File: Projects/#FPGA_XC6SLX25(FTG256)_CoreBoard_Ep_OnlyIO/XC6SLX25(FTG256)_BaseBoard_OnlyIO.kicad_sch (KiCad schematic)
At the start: 3 parts, among them J1 2309411-1, J2 Conn_01x30, J3 Conn_01x30

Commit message: update FPGA_XC6SLX25_BaseBoard_OnlyIO
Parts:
- added J4, J5: Conn_01x30, Connector_PinSocket_2.54mm:PinSocket_1x30_P2.54mm_Vertical, symbol Connector_Generic:Conn_01x30
- J2, J3: footprint (none) -> Connector_PinSocket_2.54mm:PinSocket_1x30_P2.54mm_Vertical
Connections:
- net Bank0_L1-: now also J4.25 (Pin_25)
- net Bank0_L2+: now also J4.21 (Pin_21)
- net Bank0_L2-: now also J4.22 (Pin_22)
- net Bank0_L3+: now also J4.24 (Pin_24)
- net Bank0_L3-: now also J4.23 (Pin_23)
- net Bank0_L33+: now also J4.16 (Pin_16)
- net Bank0_L33-: now also J4.15 (Pin_15)
- net Bank0_L34+: now also J4.14 (Pin_14)
- net Bank0_L34-: now also J4.13 (Pin_13)
- net Bank0_L35+: now also J4.11 (Pin_11)
- net Bank0_L35-: now also J4.12 (Pin_12)
- net Bank0_L36+: now also J5.11 (Pin_11)
- net Bank0_L36-: now also J5.10 (Pin_10)
- net Bank0_L37+: now also J5.4 (Pin_4)
- net Bank0_L37-: now also J5.5 (Pin_5)
- net Bank0_L38+: now also J5.8 (Pin_8)
- net Bank0_L38-: now also J5.9 (Pin_9)
- net Bank0_L39+: now also J4.10 (Pin_10)
- net Bank0_L39-: now also J4.9 (Pin_9)
- net Bank0_L4+: now also J4.20 (Pin_20)
- net Bank0_L4-: now also J4.19 (Pin_19)
- net Bank0_L40+: now also J5.7 (Pin_7)
- net Bank0_L40-: now also J5.6 (Pin_6)
- net Bank0_L5+: now also J5.13 (Pin_13)
- net Bank0_L5-: now also J5.12 (Pin_12)
- net Bank0_L6+: now also J4.17 (Pin_17)
- net Bank0_L6-: now also J4.18 (Pin_18)
- net Bank0_L62+: now also J4.7 (Pin_7)
- net Bank0_L62-: now also J4.8 (Pin_8)
- net Bank0_L63+: now also J3.29 (Pin_29)
- net Bank0_L63-: now also J3.28 (Pin_28)
- net Bank0_L64+: now also J5.3 (Pin_3)
- net Bank0_L64-: now also J5.2 (Pin_2)
- net Bank0_L65+: now also J4.5 (Pin_5)
- net Bank0_L65-: now also J4.6 (Pin_6)
- net Bank0_L66+: now also J5.1 (Pin_1)
- net Bank0_L66-: now also J3.30 (Pin_30)
- net Bank0_L7+: now also J5.15 (Pin_15)
- net Bank0_L7-: now also J5.14 (Pin_14)
- net Bank1_L29+: now also J4.4 (Pin_4)
- net Bank1_L29-: now also J4.3 (Pin_3)
- net Bank1_L30+: now also J3.24 (Pin_24)
- net Bank1_L30-: now also J3.25 (Pin_25)
- net Bank1_L32+: now also J3.23 (Pin_23)
- net Bank1_L32-: now also J3.22 (Pin_22)
- net Bank1_L33+: now also J4.2 (Pin_2)
- net Bank1_L33-: now also J4.1 (Pin_1)
- net Bank1_L38+: now also J3.26 (Pin_26)
- net Bank1_L38-: now also J3.27 (Pin_27)
- net Bank1_L39+: now also J3.19 (Pin_19)
- net Bank1_L39-: now also J3.18 (Pin_18)
- net Bank1_L40+: now also J3.21 (Pin_21)
- net Bank1_L40-: now also J3.20 (Pin_20)
- net Bank1_L41+: now also J3.15 (Pin_15)
- net Bank1_L41-: now also J3.14 (Pin_14)
- net Bank1_L42+: now also J3.16 (Pin_16)
- net Bank1_L42-: now also J3.17 (Pin_17)
- net Bank1_L53+: now also J3.13 (Pin_13)
- net Bank1_L53-: now also J3.12 (Pin_12)
- net Bank1_L74+: now also J3.11 (Pin_11)
- net Bank1_L74-: now also J3.10 (Pin_10)
- net Bank2_L13-: now also J3.5 (Pin_5)
- net Bank2_L14+: now also J4.28 (Pin_28)
- net Bank2_L14-: now also J4.29 (Pin_29)
- net Bank2_L16+: now also J5.22 (Pin_22)
- net Bank2_L16-: now also J5.23 (Pin_23)
- net Bank2_L23+: now also J4.30 (Pin_30)
- net Bank2_L23-: now also J5.19 (Pin_19)
- net Bank2_L29+: now also J4.26 (Pin_26)
- net Bank2_L29-: now also J4.27 (Pin_27)
- net Bank2_L30+: now also J5.21 (Pin_21)
- net Bank2_L30-: now also J5.20 (Pin_20)
- net Bank2_L31+: now also J5.24 (Pin_24)
- net Bank2_L31-: now also J5.25 (Pin_25)
- net Bank2_L32+: now also J3.3 (Pin_3)
- net Bank2_L47+: now also J3.6 (Pin_6)
- net Bank2_L47-: now also J3.2 (Pin_2)
- net Bank2_L48+: now also J3.4 (Pin_4)
- net Bank2_L48-: now also J5.30 (Pin_30)
- net Bank2_L49+: now also J5.29 (Pin_29)
- net Bank2_L49-: now also J5.28 (Pin_28)
- net Bank2_L62+: now also J5.26 (Pin_26)
- net Bank2_L62-: now also J5.27 (Pin_27)
- net Bank2_L63+: now also J3.9 (Pin_9)
- net Bank2_L63-: now also J3.1 (Pin_1)
- net Bank2_L64+: now also J3.8 (Pin_8)
- net Bank2_L64-: now also J3.7 (Pin_7)

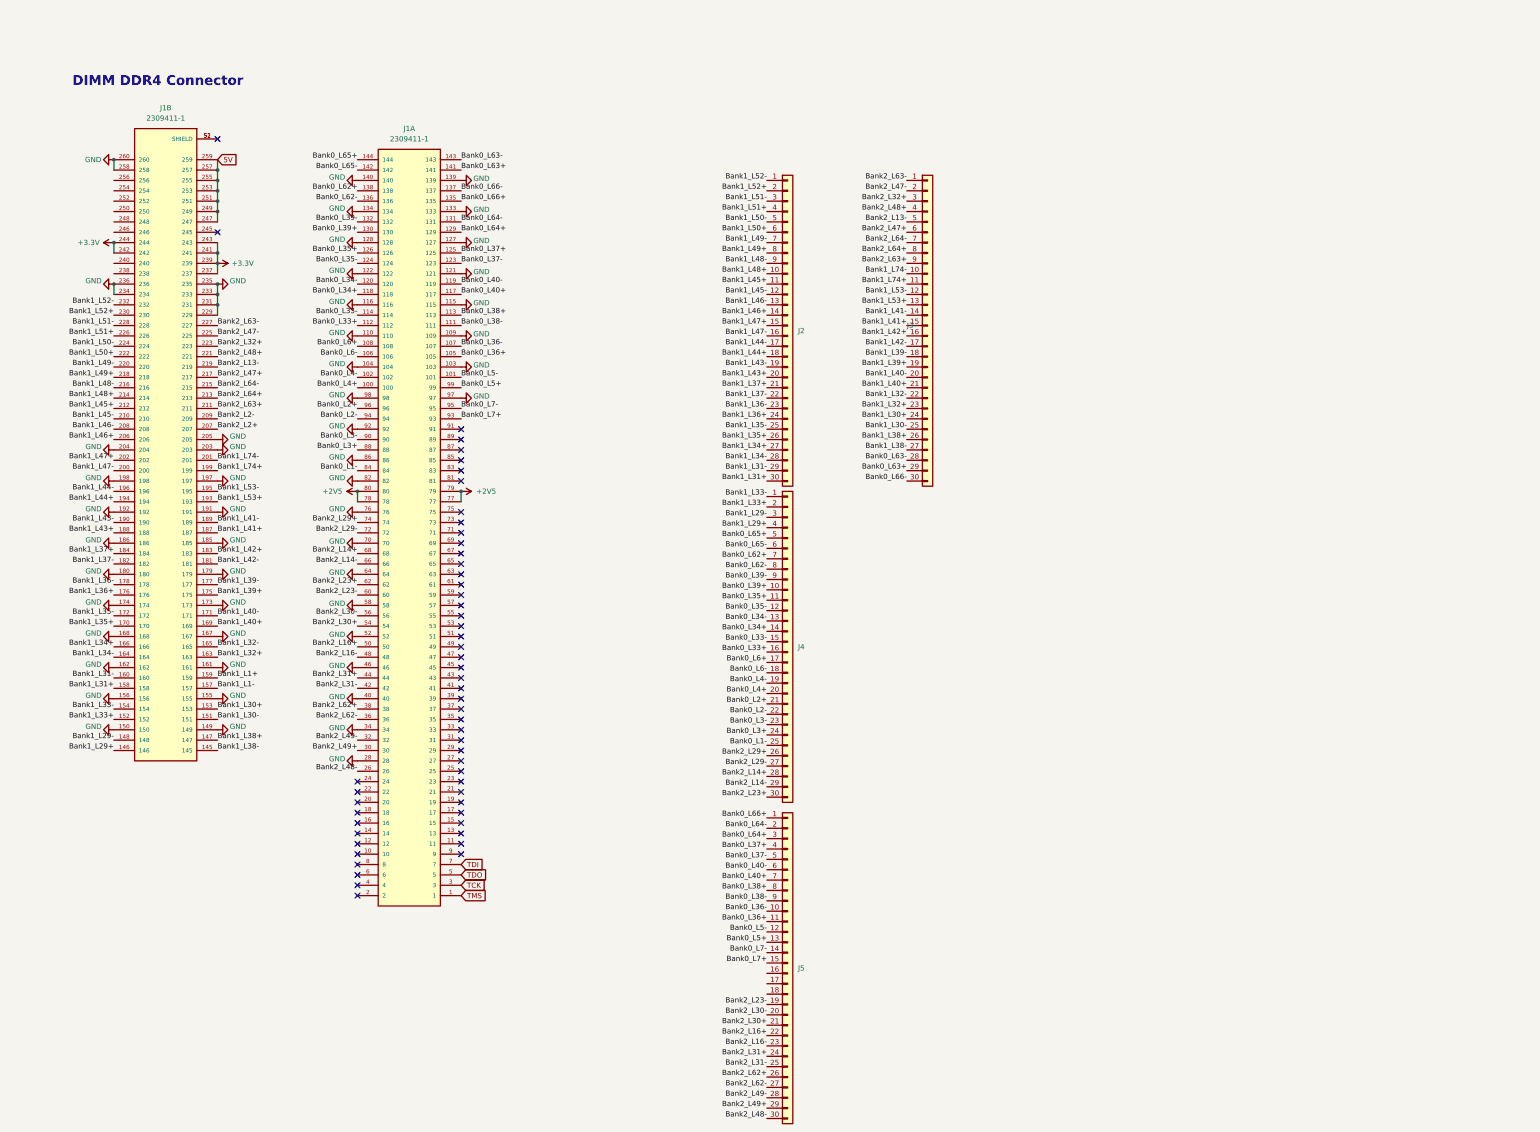
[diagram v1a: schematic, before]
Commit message: finish XC6SLX25(FTG256)_BaseBoard_OnlyIO (sample)
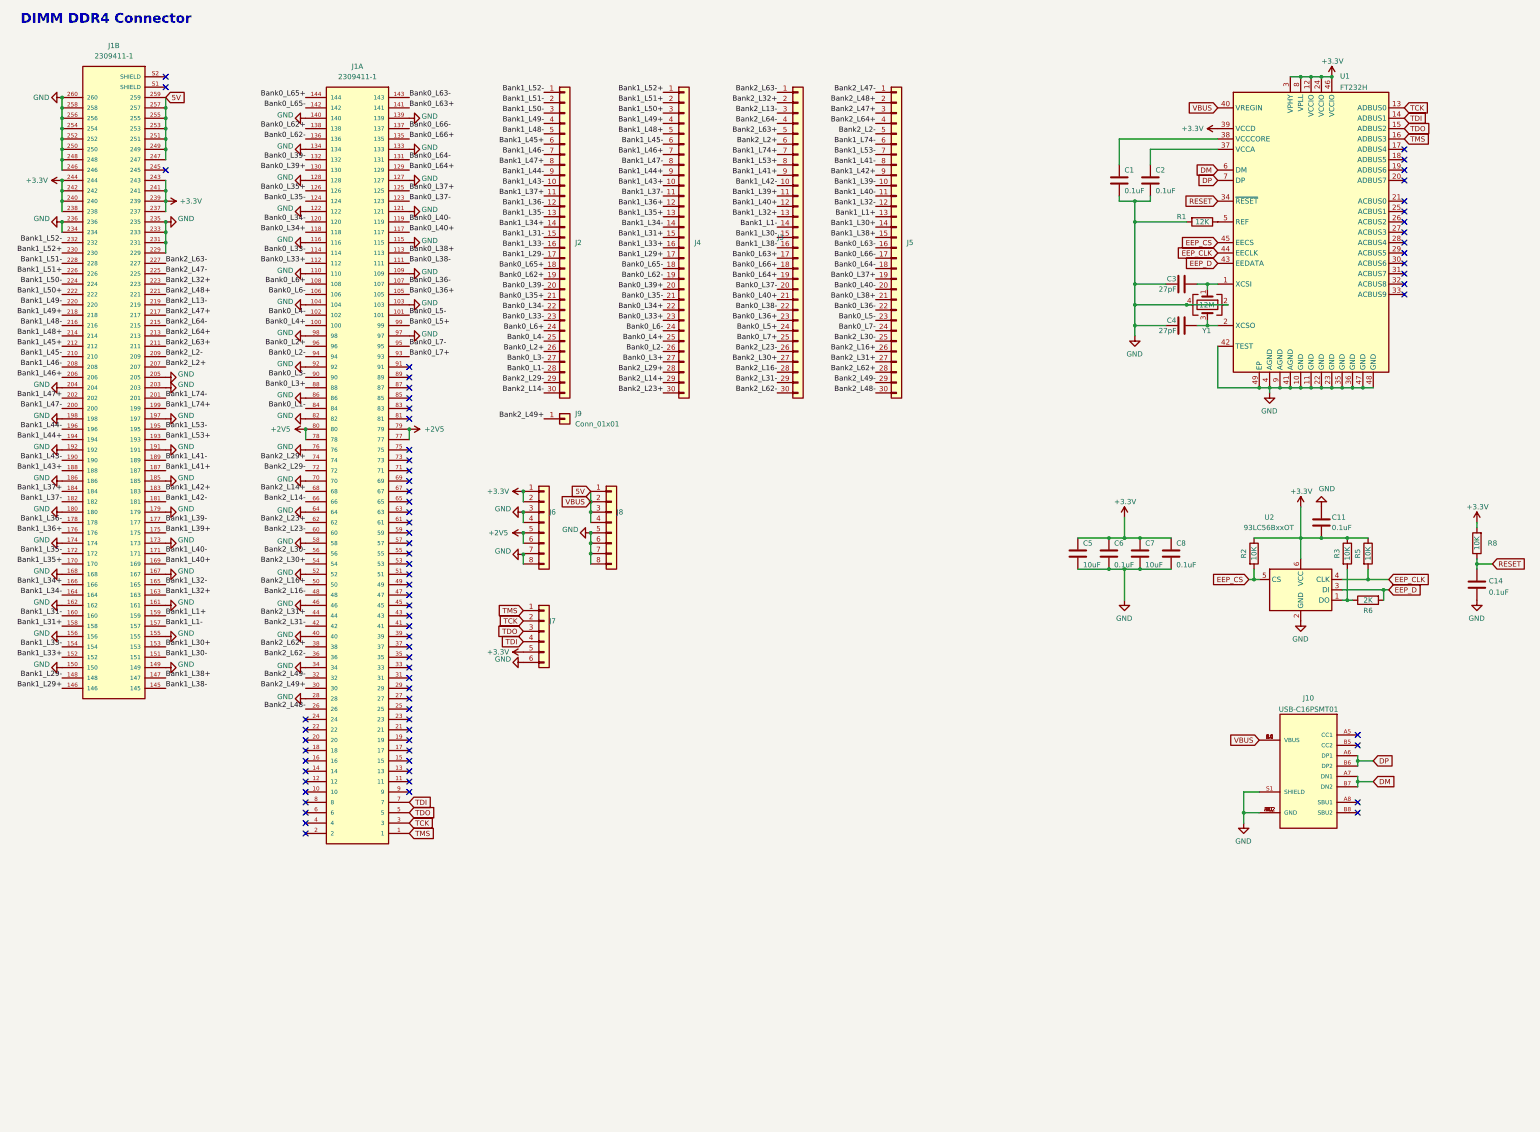
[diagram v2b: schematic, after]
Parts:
- added C1, C11, C14, C2, C6, C8: 0.1uF, Capacitor_SMD:C_0402_1005Metric, symbol Device:C
- added C3, C4: 27pF, Capacitor_SMD:C_0402_1005Metric, symbol Device:C
- added C5, C7: 10uF, Capacitor_SMD:C_0402_1005Metric, symbol Device:C
- added J10: USB-C16PSMT01, Connector_USB:USB_C_Receptacle_XKB_U262-16XN-4BVC11, symbol USB-C16PSMT01:CQ-USB-C16PSMT01
- added J6, J8: Conn_01x08, Connector_PinHeader_2.54mm:PinHeader_1x08_P2.54mm_Vertical, symbol Connector_Generic:Conn_01x08
- added J7: Conn_01x06, Connector_PinHeader_2.54mm:PinHeader_1x06_P2.54mm_Vertical, symbol Connector_Generic:Conn_01x06
- added J9: Conn_01x01, Connector_PinHeader_2.54mm:PinHeader_1x01_P2.54mm_Vertical, symbol Connector_Generic:Conn_01x01
- added R1: 12K, Resistor_SMD:R_0402_1005Metric, symbol Device:R
- added R2, R3, R5, R8: 10K, Resistor_SMD:R_0402_1005Metric, symbol Device:R
- added R6: 2K, Resistor_SMD:R_0402_1005Metric, symbol Device:R
- added U1: FT232H, Package_DFN_QFN:QFN-48-1EP_8x8mm_P0.5mm_EP6.2x6.2mm, symbol Interface_USB:FT232H
- added U2: 93LC56BxxOT, Package_TO_SOT_SMD:SOT-23-6, symbol Memory_EEPROM:93LCxxBxxOT
- added Y1: 12M, Crystal:Crystal_SMD_2016-4Pin_2.0x1.6mm, symbol Device:Crystal_GND24
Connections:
- net +2V5: now also J6.5 (Pin_5), J6.6 (Pin_6)
- net +3V3: now also J1.238, J1.240, C11.1, C5.1, C6.1, C7.1, C8.1, J6.1 (Pin_1), J6.2 (Pin_2), J7.5 (Pin_5), R2.1, R3.1, R5.1, R8.2, U1.12 (VCCIO), U1.24 (VCCIO), U1.3 (VPHY), U1.39 (VCCD), U1.46 (VCCIO), U1.8 (VPLL), U2.6 (VCC)
- net 5V: now also J10.A4 (VBUS), J10.A9 (VBUS), J10.B4 (VBUS), J10.B9 (VBUS), J8.1 (Pin_1), J8.2 (Pin_2), J8.3 (Pin_3), J8.4 (Pin_4), U1.40 (VREGIN)
- net Bank0_L1-: now also J2.28 (Pin_28); no longer J4.25 (Pin_25)
- net Bank0_L2+: now also J2.26 (Pin_26); no longer J4.21 (Pin_21)
- net Bank0_L2-: now also J4.26 (Pin_26); no longer J4.22 (Pin_22)
- net Bank0_L3+: now also J4.27 (Pin_27); no longer J4.24 (Pin_24)
- net Bank0_L3-: now also J2.27 (Pin_27); no longer J4.23 (Pin_23)
- net Bank0_L33+: now also J4.23 (Pin_23); no longer J4.16 (Pin_16)
- net Bank0_L33-: now also J2.23 (Pin_23); no longer J4.15 (Pin_15)
- net Bank0_L34+: now also J4.22 (Pin_22); no longer J4.14 (Pin_14)
- net Bank0_L34-: now also J2.22 (Pin_22); no longer J4.13 (Pin_13)
- net Bank0_L35+: now also J2.21 (Pin_21); no longer J4.11 (Pin_11)
- net Bank0_L35-: now also J4.21 (Pin_21); no longer J4.12 (Pin_12)
- net Bank0_L36+: now also J3.23 (Pin_23); no longer J5.11 (Pin_11)
- net Bank0_L36-: now also J5.22 (Pin_22); no longer J5.10 (Pin_10)
- net Bank0_L37+: now also J5.19 (Pin_19); no longer J5.4 (Pin_4)
- net Bank0_L37-: now also J3.20 (Pin_20); no longer J5.5 (Pin_5)
- net Bank0_L38+: now also J5.21 (Pin_21); no longer J5.8 (Pin_8)
- net Bank0_L38-: now also J3.22 (Pin_22); no longer J5.9 (Pin_9)
- net Bank0_L39+: now also J4.20 (Pin_20); no longer J4.10 (Pin_10)
- net Bank0_L39-: now also J2.20 (Pin_20); no longer J4.9 (Pin_9)
- net Bank0_L4+: now also J4.25 (Pin_25); no longer J4.20 (Pin_20)
- net Bank0_L4-: now also J2.25 (Pin_25); no longer J4.19 (Pin_19)
- net Bank0_L40+: now also J3.21 (Pin_21); no longer J5.7 (Pin_7)
- net Bank0_L40-: now also J5.20 (Pin_20); no longer J5.6 (Pin_6)
- net Bank0_L5+: now also J3.24 (Pin_24); no longer J5.13 (Pin_13)
- net Bank0_L5-: now also J5.23 (Pin_23); no longer J5.12 (Pin_12)
- net Bank0_L6+: now also J2.24 (Pin_24); no longer J4.17 (Pin_17)
- net Bank0_L6-: now also J4.24 (Pin_24); no longer J4.18 (Pin_18)
- net Bank0_L62+: now also J2.19 (Pin_19); no longer J4.7 (Pin_7)
- net Bank0_L62-: now also J4.19 (Pin_19); no longer J4.8 (Pin_8)
- net Bank0_L63+: now also J3.17 (Pin_17); no longer J3.29 (Pin_29)
- net Bank0_L63-: now also J5.16 (Pin_16); no longer J3.28 (Pin_28)
- net Bank0_L64+: now also J3.19 (Pin_19); no longer J5.3 (Pin_3)
- net Bank0_L64-: now also J5.18 (Pin_18); no longer J5.2 (Pin_2)
- net Bank0_L65+: now also J2.18 (Pin_18); no longer J4.5 (Pin_5)
- net Bank0_L65-: now also J4.18 (Pin_18); no longer J4.6 (Pin_6)
- net Bank0_L66+: now also J3.18 (Pin_18); no longer J5.1 (Pin_1)
- net Bank0_L66-: now also J5.17 (Pin_17); no longer J3.30 (Pin_30)
- net Bank0_L7+: now also J3.25 (Pin_25); no longer J5.15 (Pin_15)
- net Bank0_L7-: now also J5.24 (Pin_24); no longer J5.14 (Pin_14)
- net Bank1_L1+: now also J5.13 (Pin_13)
- net Bank1_L1-: now also J3.14 (Pin_14)
- net Bank1_L29+: now also J4.17 (Pin_17); no longer J4.4 (Pin_4)
- net Bank1_L29-: now also J2.17 (Pin_17); no longer J4.3 (Pin_3)
- net Bank1_L30+: now also J5.14 (Pin_14); no longer J3.24 (Pin_24)
- net Bank1_L30-: now also J3.15 (Pin_15); no longer J3.25 (Pin_25)
- net Bank1_L31+: now also J4.15 (Pin_15); no longer J2.30 (Pin_30)
- net Bank1_L31-: now also J2.15 (Pin_15); no longer J2.29 (Pin_29)
- net Bank1_L32+: now also J3.13 (Pin_13); no longer J3.23 (Pin_23)
- net Bank1_L32-: now also J5.12 (Pin_12); no longer J3.22 (Pin_22)
- net Bank1_L33+: now also J4.16 (Pin_16); no longer J4.2 (Pin_2)
- net Bank1_L33-: now also J2.16 (Pin_16); no longer J4.1 (Pin_1)
- net Bank1_L34+: now also J2.14 (Pin_14); no longer J2.27 (Pin_27)
- net Bank1_L34-: now also J4.14 (Pin_14); no longer J2.28 (Pin_28)
- net Bank1_L35+: now also J4.13 (Pin_13); no longer J2.26 (Pin_26)
- net Bank1_L35-: now also J2.13 (Pin_13); no longer J2.25 (Pin_25)
- net Bank1_L36+: now also J4.12 (Pin_12); no longer J2.24 (Pin_24)
- net Bank1_L36-: now also J2.12 (Pin_12); no longer J2.23 (Pin_23)
- net Bank1_L37+: now also J2.11 (Pin_11); no longer J2.21 (Pin_21)
- net Bank1_L37-: now also J4.11 (Pin_11); no longer J2.22 (Pin_22)
- net Bank1_L38+: now also J5.15 (Pin_15); no longer J3.26 (Pin_26)
- net Bank1_L38-: now also J3.16 (Pin_16); no longer J3.27 (Pin_27)
- net Bank1_L39+: now also J3.11 (Pin_11); no longer J3.19 (Pin_19)
- net Bank1_L39-: now also J5.10 (Pin_10); no longer J3.18 (Pin_18)
- net Bank1_L40+: now also J3.12 (Pin_12); no longer J3.21 (Pin_21)
- net Bank1_L40-: now also J5.11 (Pin_11); no longer J3.20 (Pin_20)
- net Bank1_L41+: now also J3.9 (Pin_9); no longer J3.15 (Pin_15)
- net Bank1_L41-: now also J5.8 (Pin_8); no longer J3.14 (Pin_14)
- net Bank1_L42+: now also J5.9 (Pin_9); no longer J3.16 (Pin_16)
- net Bank1_L42-: now also J3.10 (Pin_10); no longer J3.17 (Pin_17)
- net Bank1_L43+: now also J4.10 (Pin_10); no longer J2.20 (Pin_20)
- net Bank1_L43-: now also J2.10 (Pin_10); no longer J2.19 (Pin_19)
- net Bank1_L44+: now also J4.9 (Pin_9); no longer J2.18 (Pin_18)
- net Bank1_L44-: now also J2.9 (Pin_9); no longer J2.17 (Pin_17)
- net Bank1_L45+: now also J2.6 (Pin_6); no longer J2.11 (Pin_11)
- net Bank1_L45-: now also J4.6 (Pin_6); no longer J2.12 (Pin_12)
- net Bank1_L46+: now also J4.7 (Pin_7); no longer J2.14 (Pin_14)
- net Bank1_L46-: now also J2.7 (Pin_7); no longer J2.13 (Pin_13)
- net Bank1_L47+: now also J2.8 (Pin_8); no longer J2.15 (Pin_15)
- net Bank1_L47-: now also J4.8 (Pin_8); no longer J2.16 (Pin_16)
- net Bank1_L48+: now also J4.5 (Pin_5); no longer J2.10 (Pin_10)
- net Bank1_L48-: now also J2.5 (Pin_5); no longer J2.9 (Pin_9)
- net Bank1_L49+: now also J4.4 (Pin_4); no longer J2.8 (Pin_8)
- net Bank1_L49-: now also J2.4 (Pin_4); no longer J2.7 (Pin_7)
- net Bank1_L50+: now also J4.3 (Pin_3); no longer J2.6 (Pin_6)
- net Bank1_L50-: now also J2.3 (Pin_3); no longer J2.5 (Pin_5)
- net Bank1_L51+: now also J4.2 (Pin_2); no longer J2.4 (Pin_4)
- net Bank1_L51-: now also J2.2 (Pin_2); no longer J2.3 (Pin_3)
- net Bank1_L52+: now also J4.1 (Pin_1); no longer J2.2 (Pin_2)
- net Bank1_L53+: now also J3.8 (Pin_8); no longer J3.13 (Pin_13)
- net Bank1_L53-: now also J5.7 (Pin_7); no longer J3.12 (Pin_12)
- net Bank1_L74+: now also J3.7 (Pin_7); no longer J3.11 (Pin_11)
- net Bank1_L74-: now also J5.6 (Pin_6); no longer J3.10 (Pin_10)
- net Bank2_L13-: now also J3.3 (Pin_3); no longer J3.5 (Pin_5)
- net Bank2_L14+: now also J4.29 (Pin_29); no longer J4.28 (Pin_28)
- net Bank2_L14-: now also J2.30 (Pin_30); no longer J4.29 (Pin_29)
- net Bank2_L16+: now also J5.26 (Pin_26); no longer J5.22 (Pin_22)
- net Bank2_L16-: now also J3.28 (Pin_28); no longer J5.23 (Pin_23)
- net Bank2_L2+: now also J3.6 (Pin_6)
- net Bank2_L2-: now also J5.5 (Pin_5)
- net Bank2_L23-: now also J3.26 (Pin_26); no longer J5.19 (Pin_19)
- net Bank2_L29+: now also J4.28 (Pin_28); no longer J4.26 (Pin_26)
- net Bank2_L29-: now also J2.29 (Pin_29); no longer J4.27 (Pin_27)
- net Bank2_L30+: now also J3.27 (Pin_27); no longer J5.21 (Pin_21)
- net Bank2_L30-: now also J5.25 (Pin_25); no longer J5.20 (Pin_20)
- net Bank2_L31+: now also J5.27 (Pin_27); no longer J5.24 (Pin_24)
- net Bank2_L31-: now also J3.29 (Pin_29); no longer J5.25 (Pin_25)
- net Bank2_L32+: now also J3.2 (Pin_2); no longer J3.3 (Pin_3)
- net Bank2_L47+: now also J5.3 (Pin_3); no longer J3.6 (Pin_6)
- net Bank2_L47-: now also J5.1 (Pin_1); no longer J3.2 (Pin_2)
- net Bank2_L48+: now also J5.2 (Pin_2); no longer J3.4 (Pin_4)
- net Bank2_L49+: now also J9.1 (Pin_1); no longer J5.29 (Pin_29)
- net Bank2_L49-: now also J5.29 (Pin_29); no longer J5.28 (Pin_28)
- net Bank2_L62+: now also J5.28 (Pin_28); no longer J5.26 (Pin_26)
- net Bank2_L62-: now also J3.30 (Pin_30); no longer J5.27 (Pin_27)
- net Bank2_L63+: now also J3.5 (Pin_5); no longer J3.9 (Pin_9)
- net Bank2_L64+: now also J5.4 (Pin_4); no longer J3.8 (Pin_8)
- net Bank2_L64-: now also J3.4 (Pin_4); no longer J3.7 (Pin_7)
- net GND: now also J1.246, J1.248, J1.250, J1.252, J1.254, J1.256, C1.2, C11.2, C14.2, C2.2, C3.1, C4.1, C5.2, C6.2, C7.2, C8.2, J10.A1 (GND), J10.A12 (GND), J10.B1 (GND), J10.B12 (GND), J10.S1 (SHIELD), J6.3 (Pin_3), J6.4 (Pin_4), J6.7 (Pin_7), J6.8 (Pin_8), J7.6 (Pin_6), J8.5 (Pin_5), J8.6 (Pin_6), J8.7 (Pin_7), J8.8 (Pin_8), R1.2, U1.10 (GND), U1.11 (GND), U1.22 (GND), U1.23 (GND), U1.35 (GND), U1.36 (GND), U1.4 (AGND), U1.41 (AGND), U1.42 (TEST), U1.47 (GND), U1.48 (GND), U1.49 (EP), U1.9 (AGND), U2.2 (GND), Y1.2, Y1.4
- net TCK: now also J7.2 (Pin_2), U1.13 (ADBUS0)
- net TDI: now also J7.4 (Pin_4), U1.14 (ADBUS1)
- net TDO: now also J7.3 (Pin_3), U1.15 (ADBUS2)
- net TMS: now also J7.1 (Pin_1), U1.16 (ADBUS3)
- net at J1.S1 (SHIELD): no longer J1.S2 (SHIELD)
- new net: C1.1, U1.38 (VCCCORE)
- new net: C3.2, U1.1 (XCSI), Y1.1
- new net: C4.2, U1.2 (XCSO), Y1.3
- new net: R1.1, U1.5 (REF)
- new net: C2.1, U1.37 (VCCA)
- new net: R3.2, R6.1, U2.1 (DO)
- new net DM: J10.A7 (DN1), J10.B7 (DN2), U1.6 (DM)
- new net DP: J10.A6 (DP1), J10.B6 (DP2), U1.7 (DP)
- new net EEP_CLK: R5.2, U1.44 (EECLK), U2.4 (CLK)
- new net EEP_CS: R2.2, U1.45 (EECS), U2.5 (CS)
- new net EEP_D: R6.2, U1.43 (EEDATA), U2.3 (DI)
- new net RESET: C14.1, R8.1, U1.34 (~{RESET})
- no-connect marks 54 -> 73
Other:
- moved on the sheet: J1A, J2, J3, J4, J5
